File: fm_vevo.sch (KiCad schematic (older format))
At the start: 77 parts, among them J1 Bemenet, J2 RedPitaya_OSC, J3 12VDC, J4 RedPitaya_IN, J5 AudioJack2, Q1 mmbfj310, Q2 MMBT3904, Q3 MMBT3904, Q4 MMBT3904, Q5 MMBT3904, U1 LM358

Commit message: first sa612
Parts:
- removed C10: 10n, symbol Device:C
- removed C11: 3n, symbol Device:C
- removed C14: 580p, symbol Device:C
- removed L4: 372n, symbol Device:L
- removed Q3: MMBT3904, Package_TO_SOT_SMD:SOT-23, symbol Transistor_BJT:MMBT3904
- removed R10: 6k6, symbol Device:R
- removed R11: 6k, symbol Device:R
- removed R9: 5k4, symbol Device:R
- added C? (x3): 10n, symbol Device:C
- added C? (x3): 3n, symbol Device:C
- added C?: 290p, symbol Device:C
- added C?: 1n5, symbol Device:C
- added L?: 910n, symbol Device:L
- added U?: SA612, Package_SO:SO-8_3.9x4.9mm_P1.27mm, symbol custom:SA612
- added U?: L78L06_SOT89, Package_TO_SOT_SMD:SOT-89-3, symbol Regulator_Linear:L78L06_SOT89
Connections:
- net +12V: now also C?.1, U?.3 (IN)
- net GND: now also R4.2, C?.1, C?.2, C?.2, C?.2, C?.2, C?.2, C?.2, U?.2 (GND), U?.3 (GND); no longer L3.2
- net at C5.1, Q1.2 (S): now also L3.1; no longer R4.1
- net at L2.2, Q1.1 (D): now also C?.2
- net at FL1.1 (IN): now also C?.1, L?.2
- net at C13.1: now also U?.7 (OSC_E)
- new net: C?.1, L3.2, R4.1
- new net: C?.1, U?.1 (IN_A)
- new net: C?.2, U?.2 (IN_B)
- new net: C?.1, L?.1, U?.4 (OUT_A)
- new net +6V: C?.1, C?.1, U?.1 (OUT), U?.8 (VCC)
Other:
- moved on the sheet: C13, C25, C26, C27, C4, C5, D4, D5, F1, J1, J3, L2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

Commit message: V1.2 Bement discordra és levlistára is
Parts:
- removed C1, C3, C8: 5n, symbol Device:C
- removed C16: 10n, symbol Device:C
- removed C9: dnp, symbol Device:C
- removed D1: mv7404, symbol Device:D_Capacitance
- removed L1: 1u, symbol Device:L
- removed L5: 85n, symbol Device:L
- removed Q2, Q4: MMBT3904, Package_TO_SOT_SMD:SOT-23, symbol Transistor_BJT:MMBT3904
- removed R12: 100k, symbol Device:R
- removed R2: 30k, symbol Device:R
- removed R7: 1k, symbol Device:R
- removed U?: L78L06_SOT89, Package_TO_SOT_SMD:SOT-89-3, symbol Regulator_Linear:L78L06_SOT89
- added C10, C20, C27: 100n, symbol Device:C
- added C14, C19, C21, C28: 3n, symbol Device:C
- added C17: 6p, symbol Device:C
- added C26: 10n, symbol Device:C
- added C4: dnp, symbol Device:C
- added D1: bat54c, symbol Device:D_Schottky
- added H1, H2, H3, H4: MountingHole_Pad, symbol Mechanical:MountingHole_Pad
- added J3: RedPitaya_+-10V, symbol Connector:Conn_Coaxial
- added L3: 60n, symbol Device:L
- added R2: 470, symbol Device:RTRIM
- added U1: LM358, symbol Amplifier_Operational:LM358
- added U3: 74LVC1GU04, symbol 74xGxx:74LVC1GU04
- added U4: 74AHC1G4210, Package_TO_SOT_SMD:SOT-353_SC-70-5, symbol 74xGxx:74AHC1G4210
- added U6: L78L05_SO8, Package_SO:SOIC-8_3.9x4.9mm_P1.27mm, symbol Regulator_Linear:L78L05_SO8
- C12: value 5n -> 20p
- C15: value 36p -> 7p
- C2: value 200p -> 100n
- C25: renamed from C20; value 340p -> 330p
- C31: renamed from C22; value 10n -> 3n
- C6: value 10n -> 100n
- C7: value 5n -> 10n
- D2: value mv7404 -> bby40
- J1: renamed from J2; value RedPitaya_OSC -> RedPitaya_kimenete
- J5: renamed from J4; value RedPitaya_IN -> RedPitaya_+-1V
- R1: value 50k -> 200
- R3: value 8k -> 10k
- R4: value 200 -> 110k
- R5: value 100k -> 10k
- R6: value 13k -> 1M
- R8: value 20 -> 1M
- gave numbers to parts that had none: 10
- renumbered C4 to C1, C17 to C22, C18 to C23, C19 to C24, C21 to C29, C25 to C30, C23 to C32, C26 to C33, C24 to C34, C27 to C35, C28 to C36, C30 to C38, C29 to C39, J1 to J2, J3 to J4, J5 to J6, L2 to L1, L3 to L2, L6 to L5, L7 to L6, Q5 to Q2, R15 to R10, R16 to R11, R17 to R12, R18 to R13, R19 to R14, R20 to R15, R21 to R16, R13 to R7, R14 to R9, U1 to U5
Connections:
- net +12V: now also C7.1, RV1.3, U1.8 (V+), U6.8 (IN); no longer C15.1, C6.1, R5.1
- net GND: now also C12.2, C7.2, R3.2, RV1.1, C10.2, C17.2, C26.2, C27.1, C28.2, D1.2 (A), H1.1, H2.1, H3.1, H4.1, J3.2 (Ext), L3.2, R2.2, U1.4 (V-), U3.3 (GND), U4.3 (GND), U6.2 (GND), U6.3 (GND), U6.6 (GND), U6.7 (GND); no longer R3.1, R4.2, R6.2, R8.2
- net at C5.2, J2.1 (In): now also C4.2
- net at C3.1, L2.2: now also R2.1; no longer R4.1
- net at C8.2, L1.2, Q1.1 (D): now also C4.1
- net at R8.1: now also C21.1, U4.1 (X1)
- net at R1.2: now also J1.1 (In); no longer C2.1
- net at D2.1 (K): now also C12.1, R5.1, C14.2; no longer C7.2
- net at RV1.2: now also R5.2, C10.1, U1.1, U1.2 (-); no longer R1.1
- net at C15.2: now also C13.1, U2.6 (OSC_B); no longer C13.2
- net at C31.1, C32.2, D3.1 (K)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: now also C28.1
- net at U2.7 (OSC_E): now also C15.1, C17.1, C19.1; no longer C13.1
- net +6V renamed +5V
- net +5V: now also C26.1, C27.2, U3.5 (VCC), U4.5 (VCC), U6.1 (OUT)
- new net: C2.1, C6.1, D1.1 (K), R1.1, U1.5 (+)
- new net: C13.2, C14.1, L3.1
- new net: C19.2, R6.2, U3.2
- new net: C21.2, R6.1, U3.4
- new net: R4.2, U1.3 (+), U1.7
- new net: R3.1, R4.1, U1.6 (-)
- new net: R8.2, U4.2 (X2)
- new net: C20.2, U4.4 (Q)
- new net: C20.1, J3.1 (In)
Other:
- note added: "3,5 pF\nC_i"
- note added: "Detektoros\nváltozathoz:\nL=750 nH"
- note added: "Helyi oszcillátor"
- note added: "Kézi HO hangoló"
- note added: "RedPitaya HO visszacsatolás"
- note added: "Redpitaya HO hangoló"
- note added: "Tápegység"
- note added: "Univerzális Redpitaya és analóg FM vevő"
- note removed: "19,8 - 23,8MHz"
- note removed: "40p kellene, de elég ennyi, mert\nvan 4 pF kollektorkapacitás"
- note removed: "Detektoros változat\nHelyi oszcillátor"
- note removed: "Detektoros\nváltozathoz:\nL=750 nH\nC=300 pF"
- note removed: "Frekvencia négyszerező"
- moved on the sheet: C1, C29, C31, C32, C34, C39, J1, J5, J6, L6, R12, R13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

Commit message: Footprints nearly assosiated
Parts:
- added C41: 18p, Capacitor_SMD:C_0805_2012Metric_Pad1.15x1.40mm_HandSolder, symbol Device:C
- added J2: bemenet2, TerminalBlock:TerminalBlock_bornier-2_P5.08mm, symbol Connector:Screw_Terminal_01x02
- C1, C10, C11, C18, C2, C20, C25, C26, C27, C33, C36, C37, C4, C40, C6, C7: footprint (none) -> Capacitor_SMD:C_0805_2012Metric_Pad1.15x1.40mm_HandSolder
- C12: value 20p -> 18p; footprint (none) -> Capacitor_SMD:C_0805_2012Metric_Pad1.15x1.40mm_HandSolder
- C13, C14, C19, C23, C24, C28, C3, C31, C35, C5, C8, C9: value 3n -> 2n7; footprint (none) -> Capacitor_SMD:C_0805_2012Metric_Pad1.15x1.40mm_HandSolder
- C15: value 7p -> 6p8; footprint (none) -> Capacitor_SMD:C_0805_2012Metric_Pad1.15x1.40mm_HandSolder
- C16: value 290p -> 270p; footprint (none) -> Capacitor_SMD:C_0805_2012Metric_Pad1.15x1.40mm_HandSolder
- C17: value 6p -> 6p8; footprint (none) -> Capacitor_SMD:C_0805_2012Metric_Pad1.15x1.40mm_HandSolder
- C21: renamed from C22; footprint (none) -> Capacitor_SMD:C_0805_2012Metric_Pad1.15x1.40mm_HandSolder
- C22: renamed from C21; value 3n -> 2n7; footprint (none) -> Capacitor_SMD:C_0805_2012Metric_Pad1.15x1.40mm_HandSolder
- C29: value 3n -> 10n; footprint (none) -> Capacitor_SMD:C_0805_2012Metric_Pad1.15x1.40mm_HandSolder
- C30: footprint (none) -> Capacitor_THT:CP_Radial_D8.0mm_P3.50mm
- C32: value 150n -> 100n; footprint (none) -> Capacitor_SMD:C_0805_2012Metric_Pad1.15x1.40mm_HandSolder
- C34, C38, C39: footprint (none) -> Capacitor_THT:CP_Radial_D5.0mm_P2.00mm
- D1, D3, D4: value bat54c -> bas85; footprint (none) -> Diode_SMD:D_MiniMELF_Handsoldering
- D2: footprint (none) -> Diode_SMD:D_SOT-23_ANK
- D5: footprint (none) -> LED_SMD:LED_1206_3216Metric_Pad1.42x1.75mm_HandSolder
- F1: footprint (none) -> Fuse:Fuse_1812_4532Metric_Pad1.30x3.40mm_HandSolder
- FL1: footprint Filter:Filter_Mini-Circuits_FV1206-4 -> (none)
- H1, H2, H3, H4: footprint (none) -> MountingHole:MountingHole_3mm_Pad
- J1: footprint (none) -> Connector_Coaxial:SMA_Amphenol_132289_EdgeMount
- J3: renamed from J2; footprint (none) -> Connector_Coaxial:SMA_Amphenol_132289_EdgeMount
- J4: renamed from J3; footprint (none) -> Connector_Coaxial:SMA_Amphenol_132289_EdgeMount
- J5: renamed from J4; footprint (none) -> Connector_BarrelJack:BarrelJack_Wuerth_6941xx301002
- J6: renamed from J5; footprint (none) -> Connector_Coaxial:SMA_Amphenol_132289_EdgeMount
- J7: renamed from J6; value AudioJack2 -> AudioJack; footprint (none) -> custom:js35-09
- L1, L2, L4: footprint (none) -> Inductor_SMD:L_0805_2012Metric_Pad1.15x1.40mm_HandSolder
- L3: value 60n -> 68n; footprint (none) -> Inductor_SMD:L_0805_2012Metric_Pad1.15x1.40mm_HandSolder
- L5, L6: footprint (none) -> Inductor_SMD:L_1210_3225Metric_Pad1.42x2.65mm_HandSolder
- Q1: footprint (none) -> Package_TO_SOT_SMD:SOT-23_Handsoldering
- Q2: footprint Package_TO_SOT_SMD:SOT-23 -> Package_TO_SOT_SMD:SOT-23_Handsoldering
- R1, R11, R3, R4, R6, R8: footprint (none) -> Resistor_SMD:R_0805_2012Metric_Pad1.15x1.40mm_HandSolder
- R10: value 6k6 -> 10k; footprint (none) -> Resistor_SMD:R_0805_2012Metric_Pad1.15x1.40mm_HandSolder
- R12, R13: value 100k -> 110k; footprint (none) -> Resistor_SMD:R_0805_2012Metric_Pad1.15x1.40mm_HandSolder
- R14: value 1k -> 1k5; footprint (none) -> Resistor_SMD:R_0805_2012Metric_Pad1.15x1.40mm_HandSolder
- R15, R2, RV1: footprint (none) -> Potentiometer_THT:Potentiometer_Piher_PT-15-V02_Vertical
- R16: value 2k -> 1k5; footprint (none) -> Resistor_SMD:R_0805_2012Metric_Pad1.15x1.40mm_HandSolder
- R5: value 10k -> 68k1; footprint (none) -> Resistor_SMD:R_0805_2012Metric_Pad1.15x1.40mm_HandSolder
- R7: value 70k -> 68k1; footprint (none) -> Resistor_SMD:R_0805_2012Metric_Pad1.15x1.40mm_HandSolder
- R9: value 5k4 -> 8k2; footprint (none) -> Resistor_SMD:R_0805_2012Metric_Pad1.15x1.40mm_HandSolder
- U1, U5: footprint (none) -> Package_SO:SOIC-8_3.9x4.9mm_P1.27mm
- U3: footprint (none) -> Package_TO_SOT_SMD:SOT-353_SC-70-5_Handsoldering
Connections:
- net +12V: now also C41.1
- net GND: now also J2.1 (Pin_1)
- net at C4.2, C5.2, J3.1 (In): now also J2.2 (Pin_2)
- net at C25.2, D3.2 (A), L5.2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: now also C41.2
- no-connect marks 0 -> 1
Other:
- note added: "C41 Csak detektoroshoz!"
- note added: "Univerzális, Redpitaya és analóg FM vevő"
- note removed: "Detektoros\nváltozathoz:\nL=750 nH"
- note removed: "Univerzális Redpitaya és analóg FM vevő"
- moved on the sheet: C21, C25, L5

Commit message: PCB v0.9
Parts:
- removed C4: dnp, Capacitor_SMD:C_0805_2012Metric_Pad1.15x1.40mm_HandSolder, symbol Device:C
- FL1: footprint (none) -> custom:sfj10.7ma
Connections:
- net at C16.1, L4.1: now also U2.5 (OUT_B); no longer U2.4 (OUT_A)
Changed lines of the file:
@@
 F 0 "FL1" H 5100 2117 50  0000 C CNN
 F 1 "sfj10.7ma" H 5100 2026 50  0000 C CNN
-F 2 "" H 5100 2150 50  0001 C CNN
+F 2 "custom:sfj10.7ma" H 5100 2150 50  0001 C CNN
 F 3 "" H 5100 1750 50  0001 C CNN
 	1    5100 1650
@@
 $EndComp
 Wire Wire Line
-	3800 1800 3950 1800
-Wire Wire Line
-	3950 1800 3950 1650
-Wire Wire Line
 	3950 1650 4200 1650
 Connection ~ 4200 1650
@@
 Text Notes 7000 6750 0    118  ~ 0
 Univerzális, Redpitaya és analóg FM vevő
-$Comp
-L Device:C C4
-U 1 1 5ED39B46
-P 1600 1450
-F 0 "C4" V 1348 1450 50  0000 C CNN
-F 1 "dnp" V 1439 1450 50  0000 C CNN
-F 2 "Capacitor_SMD:C_0805_2012Metric_Pad1.15x1.40mm_HandSolder" H 1638 1300 50  0001 C CNN
-F 3 "~" H 1600 1450 50  0001 C CNN
-	1    1600 1450
-	0    1    1    0
-$EndComp
-Wire Wire Line
-	1450 1450 1300 1450
 Wire Wire Line
 	1300 1450 1300 1850
@@
 Wire Notes Line
 	5650 700  7400 700
-NoConn ~ 3800 1900
 $Comp
 L Connector:Screw_Terminal_01x02 J2
@@
 Wire Wire Line
 	1200 1450 1300 1450
-Connection ~ 1300 1450
 Connection ~ 7150 1650
 Wire Wire Line
@@
 Text Notes 6350 850  0    50   ~ 0
 C41  Csak detektoroshoz!
+Wire Wire Line
+	3800 1900 3950 1900
+Wire Wire Line
+	3950 1650 3950 1900
+NoConn ~ 3800 1800
 $EndSCHEMATC

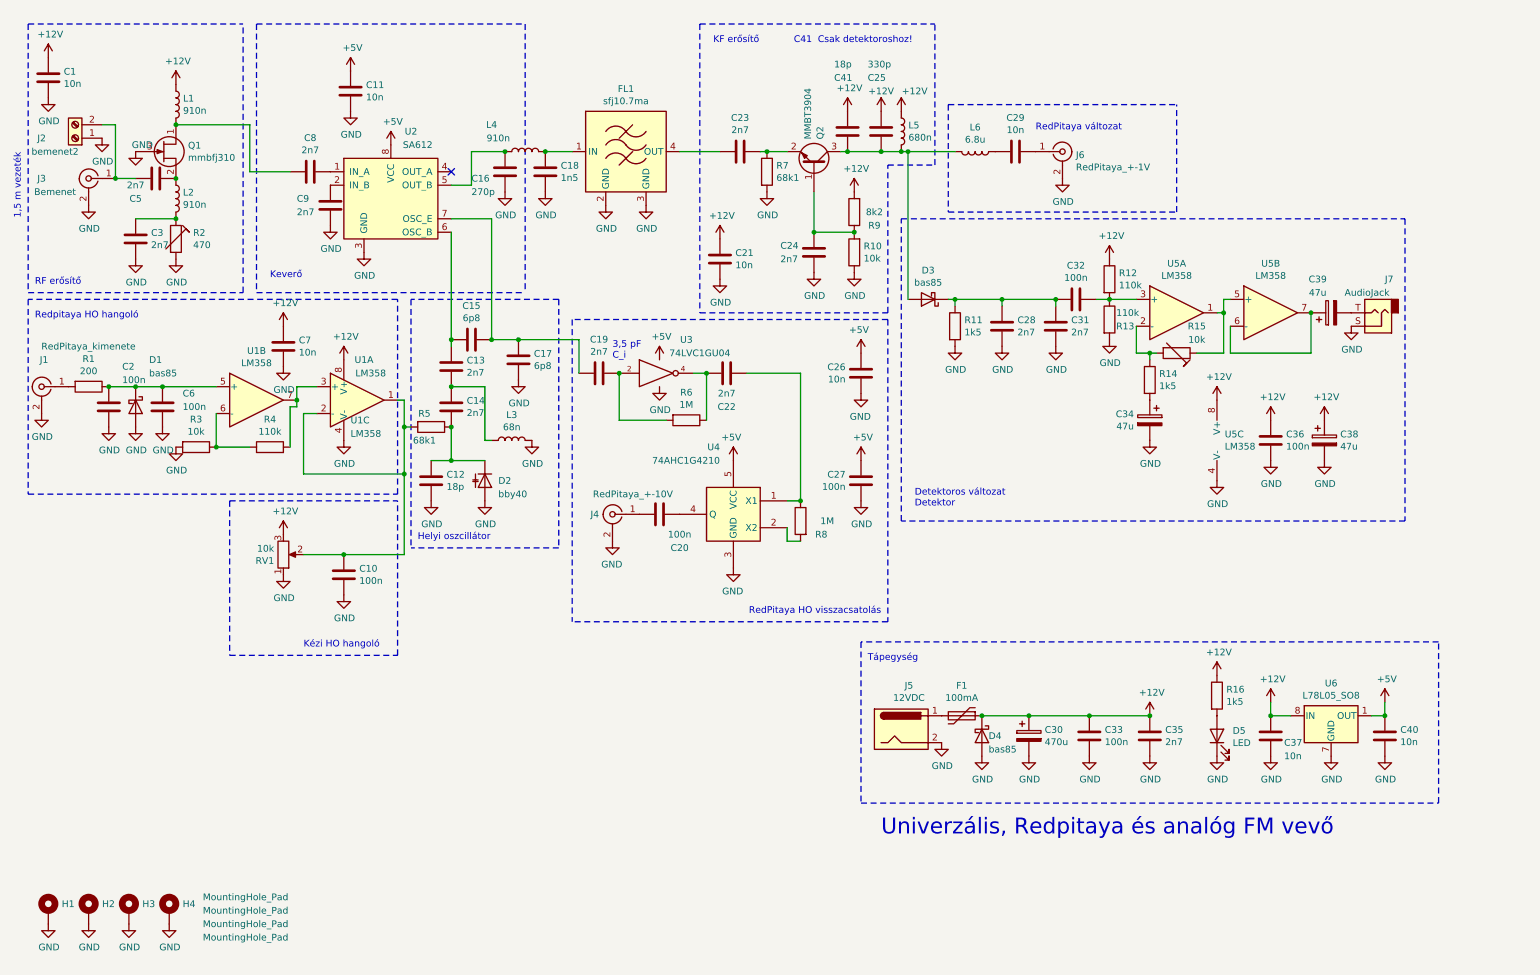
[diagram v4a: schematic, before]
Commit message: TBA120S demodulator added
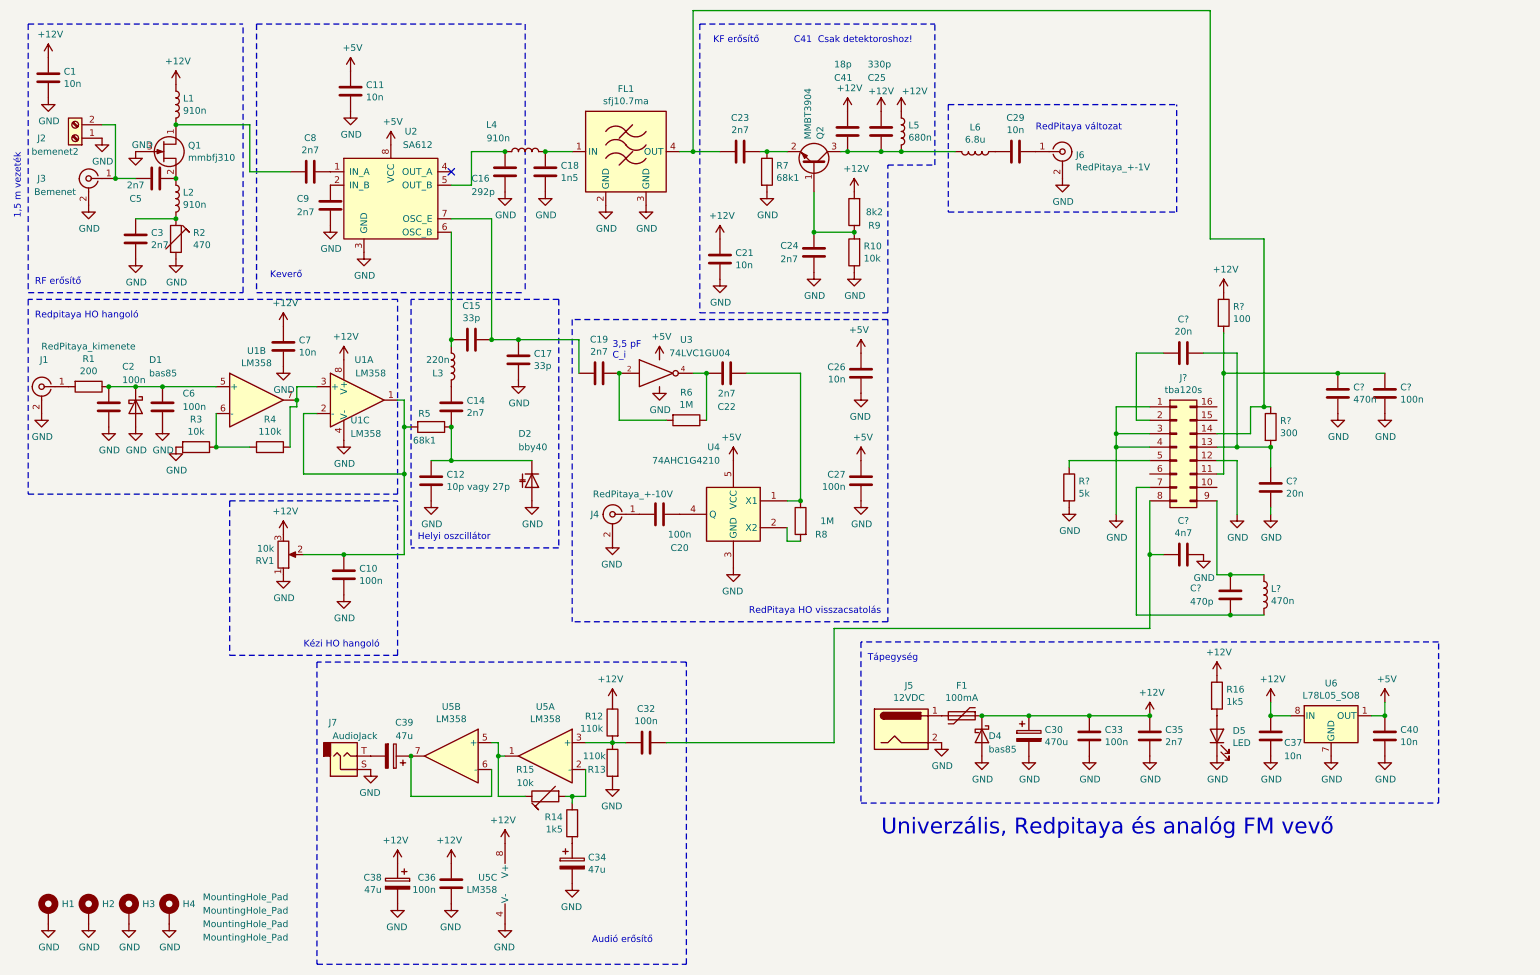
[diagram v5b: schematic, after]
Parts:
- removed C13, C28, C31: 2n7, Capacitor_SMD:C_0805_2012Metric_Pad1.15x1.40mm_HandSolder, symbol Device:C
- removed D3: bas85, Diode_SMD:D_MiniMELF_Handsoldering, symbol Device:D_Schottky
- removed R11: 1k5, Resistor_SMD:R_0805_2012Metric_Pad1.15x1.40mm_HandSolder, symbol Device:R
- added C? (x2): 20n, symbol Device:C
- added C?: 4n7, symbol Device:C
- added C?: 470p, symbol Device:C
- added C?: 100n, symbol Device:C
- added C?: 470n, symbol Device:C
- added J?: tba120s, symbol Connector_Generic:Conn_02x08_Counter_Clockwise
- added L?: 470n, symbol Device:L
- added R?: 5k, symbol Device:R
- added R?: 300, symbol Device:R
- added R?: 100, symbol Device:R
- C12: value 18p -> 10p vagy 27p
- C15, C17: value 6p8 -> 33p
- C16: value 270p -> 292p
- L3: value 68n -> 220n
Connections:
- net +12V: now also R?.1
- net GND: now also C?.1, C?.2, C?.2, C?.2, J?.1 (Pin_1), J?.12 (Pin_12), J?.3 (Pin_3), J?.4 (Pin_4), R?.2; no longer L3.2
- net at C23.2, FL1.4 (OUT): now also J?.14 (Pin_14), R?.1
- net at C32.2: now also C?.2, J?.8 (Pin_8)
- net at C15.2, U2.6 (OSC_B): now also L3.1
- net at C14.1: now also L3.2; no longer L3.1
- new net: J?.5 (Pin_5), R?.1
- new net: C?.1, C?.1, J?.11 (Pin_11), R?.2
- new net: C?.1, C?.1, J?.13 (Pin_13), R?.2
- new net: C?.2, J?.2 (Pin_2)
- new net: C?.2, J?.7 (Pin_7), L?.2
- new net: C?.1, J?.9 (Pin_9), L?.1
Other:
- note added: "Audió erősítő"
- note removed: "Detektoros változat\nDetektor"
- moved on the sheet: C32, C34, C36, C38, C39, D2, J7, L3, R12, R13, R14, R15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
